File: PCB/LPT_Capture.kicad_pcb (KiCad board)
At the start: 2 copper layers, 36 x 20.8 mm, 18 parts, among them J1 USB3155-30-A, J2 DB25P064TXLF, Q1 SL2301S, Q2 SL2301S, U1 FT245RL

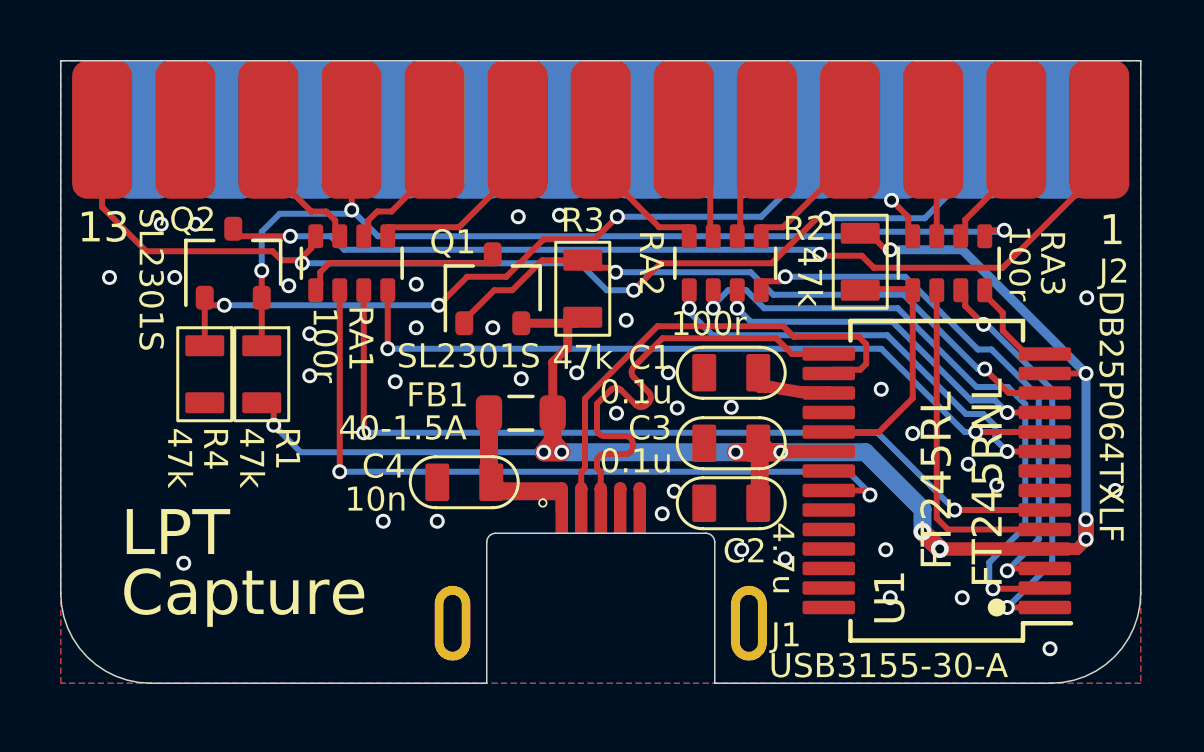
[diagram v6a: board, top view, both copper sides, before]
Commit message: vcc fewer vias, readme
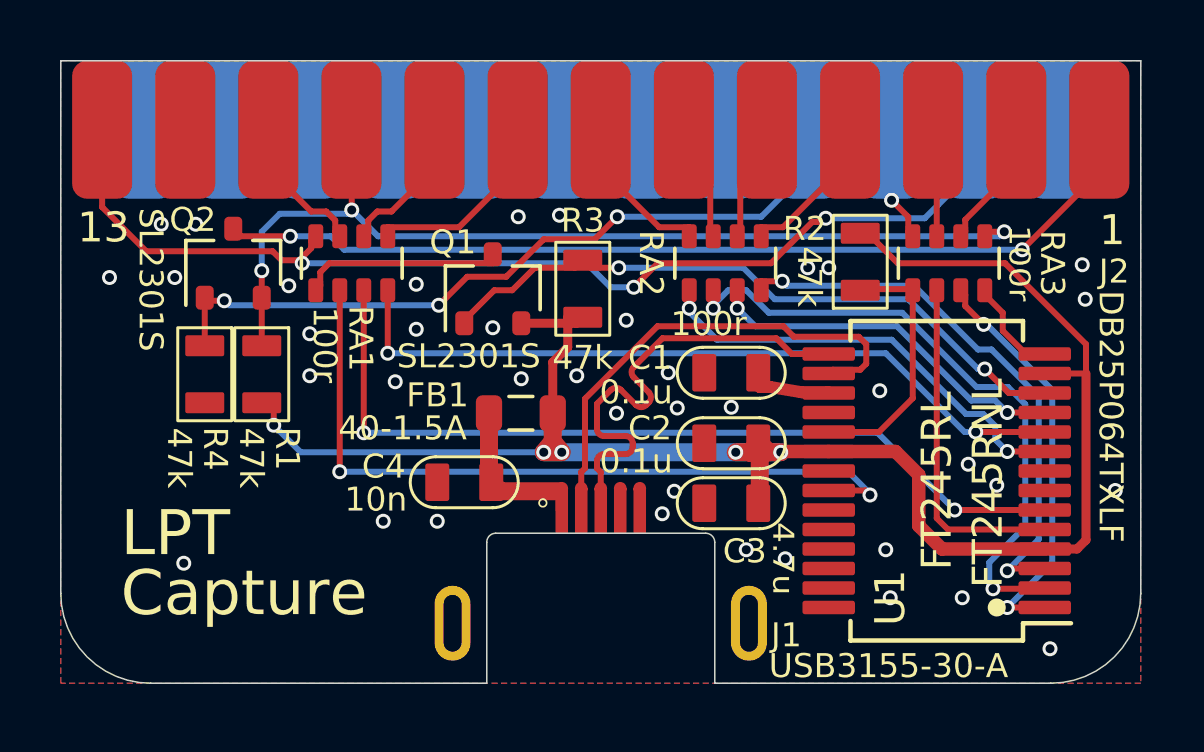
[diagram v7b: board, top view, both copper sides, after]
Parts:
- N1: value MHCCOV-25-SN-LG -> 956-025-010R031
- renumbered C3 to C2, C2 to C3
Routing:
- net VCC: track 60.6 -> 58.7 mm, vias 11 -> 5
- net GND: vias 37 -> 39
